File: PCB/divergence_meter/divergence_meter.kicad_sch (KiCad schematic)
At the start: 20 parts, among them U1 74HC595, U2 74HC595, U3 ULN2803A, U4 ULN2803A

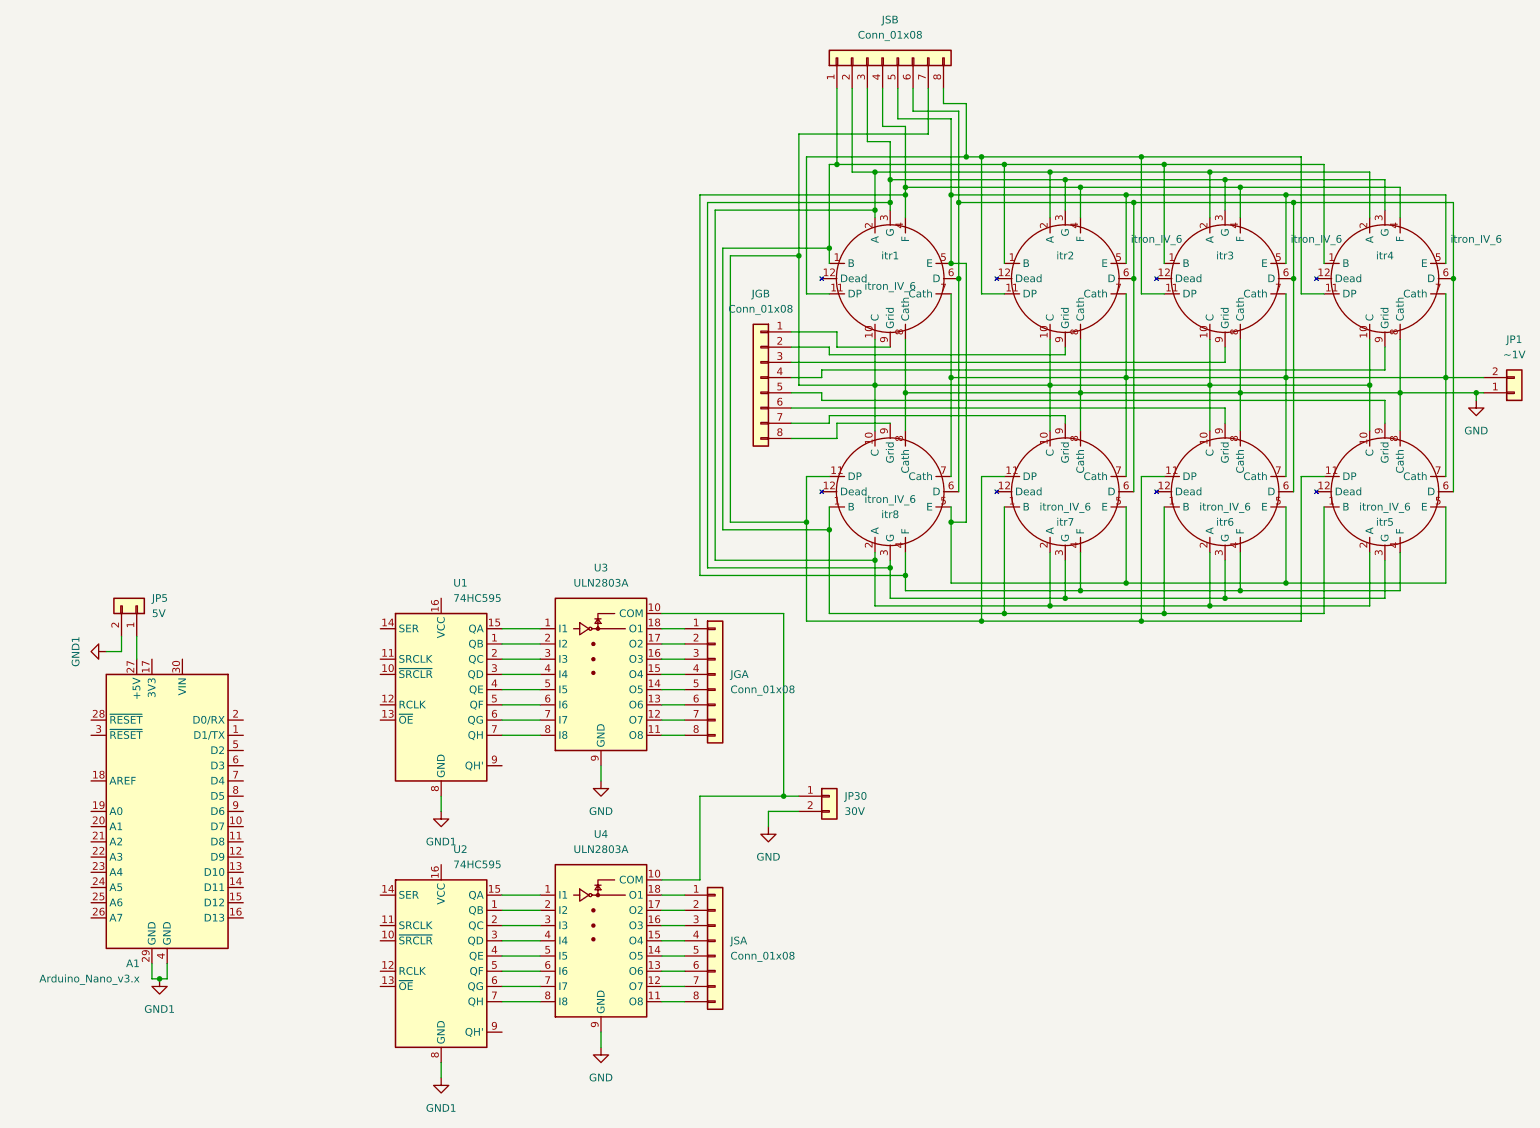
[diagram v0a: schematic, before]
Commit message: Finished schematics, started PCB design
Some schematics changes may be added
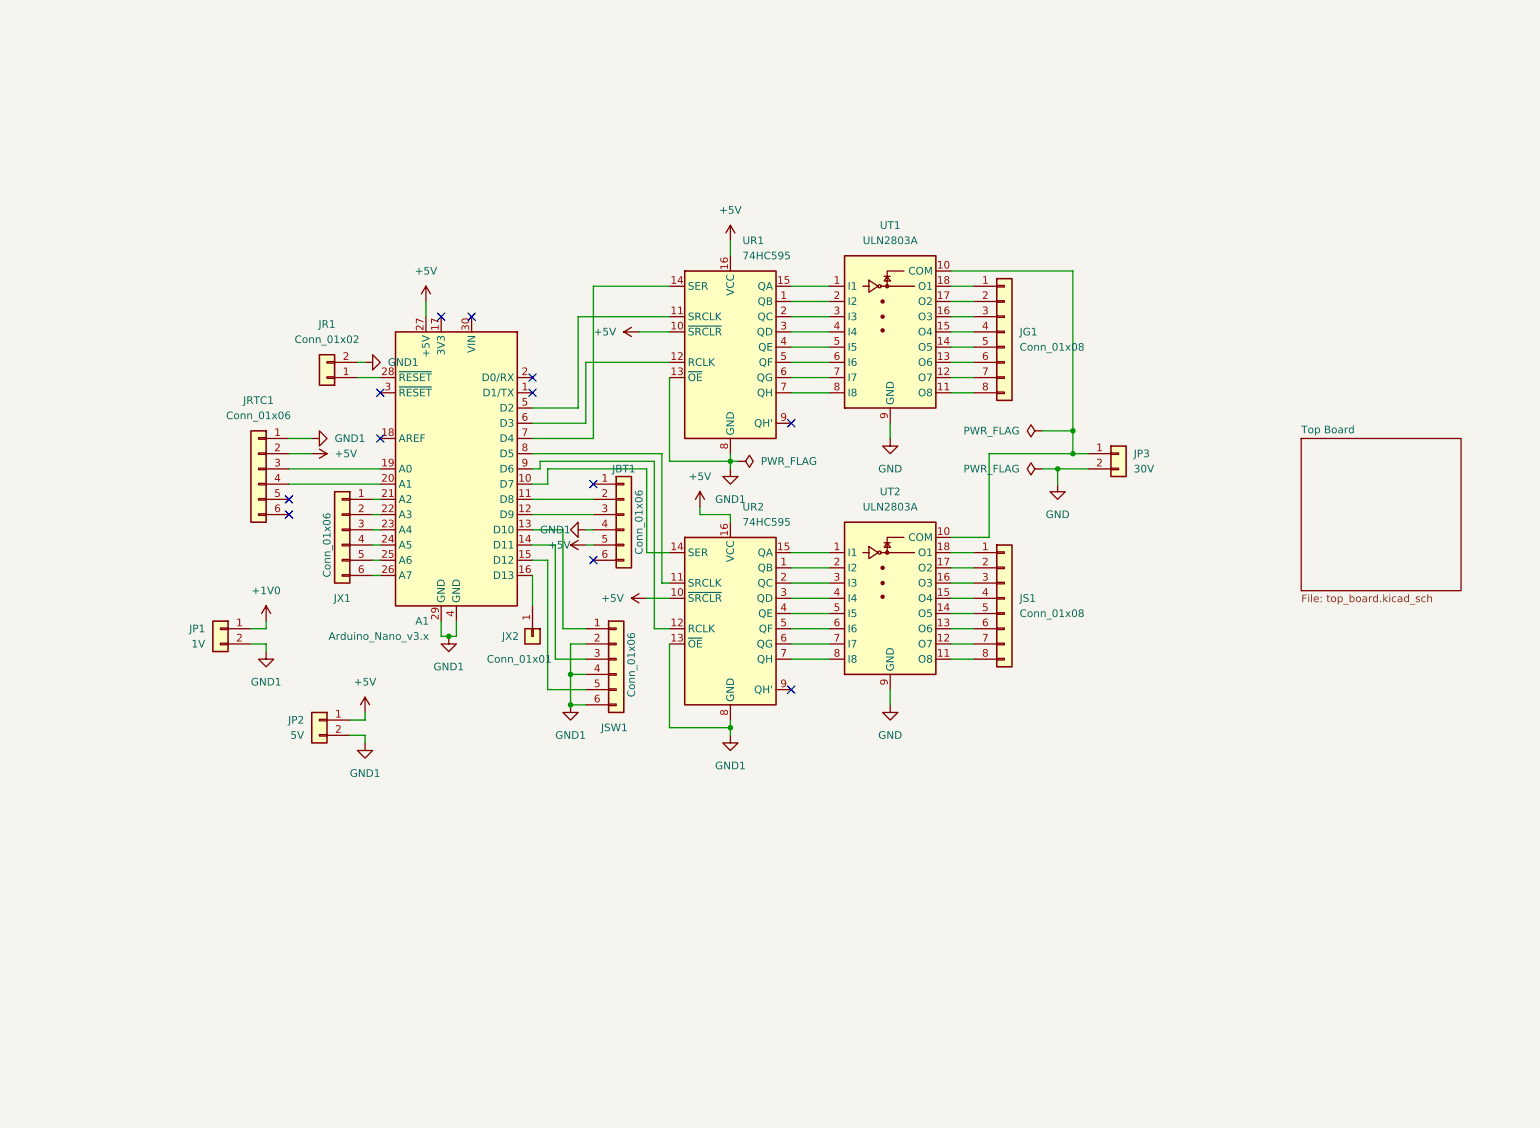
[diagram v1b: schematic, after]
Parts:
- removed JGB, JSB: Conn_01x08, symbol Connector_Generic:Conn_01x08
- removed itr1, itr2, itr3, itr4, itr5, itr6, itr7, itr8: itron_IV_6, symbol divergence:itron_IV_6
- added JBT1, JRTC1: Conn_01x06, Connector_PinSocket_1.27mm:PinSocket_1x06_P1.27mm_Vertical, symbol Connector_Generic:Conn_01x06
- added JR1: Conn_01x02, Connector_PinHeader_1.27mm:PinHeader_1x02_P1.27mm_Vertical, symbol Connector_Generic:Conn_01x02
- added JSW1, JX1: Conn_01x06, Connector_PinHeader_1.27mm:PinHeader_1x06_P1.27mm_Vertical, symbol Connector_Generic:Conn_01x06
- added JX2: Conn_01x01, Connector_PinHeader_1.27mm:PinHeader_1x01_P1.27mm_Vertical, symbol Connector_Generic:Conn_01x01
- JG1: renamed from JGA; footprint (none) -> Connector_PinHeader_1.27mm:PinHeader_1x08_P1.27mm_Vertical
- JP1: value ~1V -> 1V
- JS1: renamed from JSA; footprint (none) -> Connector_PinHeader_1.27mm:PinHeader_1x08_P1.27mm_Vertical
- UR1: renamed from U1; footprint (none) -> SN74HC595N:DIP794W53P254L1930H508Q16N
- UR2: renamed from U2; footprint (none) -> SN74HC595N:DIP794W53P254L1930H508Q16N
- UT1: renamed from U3; footprint (none) -> ULN2803A:DIP850W46P254L2324H393Q18N
- UT2: renamed from U4; footprint (none) -> ULN2803A:DIP850W46P254L2324H393Q18N
- renumbered JP5 to JP2, JP30 to JP3
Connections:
- net GND: no longer JP1.1 (Pin_1)
- net GND1: now also JP1.2 (Pin_2), UR1.13 (~{OE}), UR2.13 (~{OE}), JBT1.4 (Pin_4), JR1.2 (Pin_2), JRTC1.1 (Pin_1), JSW1.2 (Pin_2), JSW1.4 (Pin_4), JSW1.6 (Pin_6)
- net at A1.10 (D7): now also UR2.14 (SER)
- net at A1.11 (D8): now also JBT1.2 (Pin_2)
- net at A1.12 (D9): now also JBT1.3 (Pin_3)
- net at A1.13 (D10): now also JSW1.1 (Pin_1)
- net at A1.14 (D11): now also JSW1.3 (Pin_3)
- net at A1.15 (D12): now also JSW1.5 (Pin_5)
- net at A1.16 (D13): now also JX2.1 (Pin_1)
- net at A1.19 (A0): now also JRTC1.3 (Pin_3)
- net at A1.20 (A1): now also JRTC1.4 (Pin_4)
- net at A1.21 (A2): now also JX1.1 (Pin_1)
- net at A1.22 (A3): now also JX1.2 (Pin_2)
- net at A1.23 (A4): now also JX1.3 (Pin_3)
- net at A1.24 (A5): now also JX1.4 (Pin_4)
- net at A1.25 (A6): now also JX1.5 (Pin_5)
- net at A1.26 (A7): now also JX1.6 (Pin_6)
- net +5V: now reaches A1.27 (+5V), JP2.1 (Pin_1)
- net +5V: now also UR1.10 (~{SRCLR}), UR1.16 (VCC), UR2.10 (~{SRCLR}), UR2.16 (VCC), JBT1.5 (Pin_5), JRTC1.2 (Pin_2)
- net at A1.28 (~{RESET}): now also JR1.1 (Pin_1)
- net at A1.5 (D2): now also UR1.11 (SRCLK)
- net at A1.6 (D3): now also UR1.12 (RCLK)
- net at A1.7 (D4): now also UR1.14 (SER)
- net at A1.8 (D5): now also UR2.11 (SRCLK)
- net at A1.9 (D6): now also UR2.12 (RCLK)
- new net +1V0: JP1.1 (Pin_1)
- no-connect marks 0 -> 12
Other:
- added sheet Top Board (top_board.kicad_sch)
- company: (none) -> Projected by Toohka / Okarisu
- title: (none) -> Divergence Meter - logic board
- moved on the sheet: A1, JG1, JP2, JP3, JS1, UR1, UR2, UT1, UT2

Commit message: working on PCB - itron board almost done
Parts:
- added JPX1: Conn_02x04_Odd_Even, Connector_PinHeader_1.27mm:PinHeader_2x04_P1.27mm_Vertical, symbol Connector_Generic:Conn_02x04_Odd_Even
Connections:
- net +5V: now also JPX1.1 (Pin_1), JPX1.3 (Pin_3), JPX1.5 (Pin_5), JPX1.7 (Pin_7)
- net GND1: now also JPX1.2 (Pin_2), JPX1.4 (Pin_4), JPX1.6 (Pin_6), JPX1.8 (Pin_8)
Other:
- moved on the sheet: JP1, JP2

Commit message: itrons done, started logics
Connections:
- net at A1.10 (D7): now also UR2.11 (SRCLK); no longer UR2.14 (SER)
- net at A1.5 (D2): now also UR1.14 (SER); no longer UR1.11 (SRCLK)
- net at A1.7 (D4): now also UR1.11 (SRCLK); no longer UR1.14 (SER)
- net at A1.8 (D5): now also UR2.14 (SER); no longer UR2.11 (SRCLK)
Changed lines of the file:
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@@
   (no_connect (at 59.69 95.25))
   (no_connect (at 59.69 92.71))
+  (wire (pts (xy 120.65 86.36) (xy 120.65 106.68))
+    (stroke (width 0) (type default) (color 0 0 0 0))
+  )
   (wire (pts (xy 123.19 130.81) (xy 133.35 130.81))
     (stroke (width 0) (type default) (color 0 0 0 0))
   )
-  (wire (pts (xy 123.19 114.3) (xy 120.65 114.3))
-    (stroke (width 0) (type default) (color 0 0 0 0))
-  )
   (wire (pts (xy 170.18 62.23) (xy 173.99 62.23))
     (stroke (width 0) (type default) (color 0 0 0 0))
@@
     (stroke (width 0) (type default) (color 0 0 0 0))
   )
-  (wire (pts (xy 100.33 87.63) (xy 101.6 87.63))
-    (stroke (width 0) (type default) (color 0 0 0 0))
-  )
   (wire (pts (xy 170.18 114.3) (xy 173.99 114.3))
     (stroke (width 0) (type default) (color 0 0 0 0))
@@
     (stroke (width 0) (type default) (color 0 0 0 0))
   )
-  (wire (pts (xy 123.19 69.85) (xy 109.22 69.85))
+  (wire (pts (xy 100.33 90.17) (xy 104.14 90.17))
     (stroke (width 0) (type default) (color 0 0 0 0))
   )
@@
     (stroke (width 0) (type default) (color 0 0 0 0))
   )
+  (wire (pts (xy 109.22 82.55) (xy 100.33 82.55))
+    (stroke (width 0) (type default) (color 0 0 0 0))
+  )
   (wire (pts (xy 102.87 102.87) (xy 100.33 102.87))
     (stroke (width 0) (type default) (color 0 0 0 0))
@@
     (stroke (width 0) (type default) (color 0 0 0 0))
   )
-  (wire (pts (xy 123.19 101.6) (xy 119.38 101.6))
+  (wire (pts (xy 119.38 87.63) (xy 119.38 114.3))
     (stroke (width 0) (type default) (color 0 0 0 0))
   )
@@
     (stroke (width 0) (type default) (color 0 0 0 0))
   )
+  (wire (pts (xy 121.92 85.09) (xy 121.92 101.6))
+    (stroke (width 0) (type default) (color 0 0 0 0))
+  )
   (wire (pts (xy 143.51 64.77) (xy 149.86 64.77))
     (stroke (width 0) (type default) (color 0 0 0 0))
@@
     (stroke (width 0) (type default) (color 0 0 0 0))
   )
-  (wire (pts (xy 119.38 109.22) (xy 123.19 109.22))
+  (wire (pts (xy 116.84 109.22) (xy 123.19 109.22))
     (stroke (width 0) (type default) (color 0 0 0 0))
   )
@@
     (stroke (width 0) (type default) (color 0 0 0 0))
   )
-  (wire (pts (xy 101.6 87.63) (xy 101.6 86.36))
-    (stroke (width 0) (type default) (color 0 0 0 0))
-  )
   (wire (pts (xy 60.96 107.95) (xy 60.96 109.22))
     (stroke (width 0) (type default) (color 0 0 0 0))
@@
     (stroke (width 0) (type default) (color 0 0 0 0))
   )
+  (wire (pts (xy 109.22 62.23) (xy 123.19 62.23))
+    (stroke (width 0) (type default) (color 0 0 0 0))
+  )
   (wire (pts (xy 170.18 74.93) (xy 173.99 74.93))
     (stroke (width 0) (type default) (color 0 0 0 0))
@@
     (stroke (width 0) (type default) (color 0 0 0 0))
   )
-  (wire (pts (xy 123.19 62.23) (xy 107.95 62.23))
-    (stroke (width 0) (type default) (color 0 0 0 0))
-  )
-  (wire (pts (xy 120.65 86.36) (xy 120.65 114.3))
-    (stroke (width 0) (type default) (color 0 0 0 0))
-  )
   (wire (pts (xy 190.5 85.09) (xy 193.04 85.09))
     (stroke (width 0) (type default) (color 0 0 0 0))
@@
     (stroke (width 0) (type default) (color 0 0 0 0))
   )
+  (wire (pts (xy 110.49 69.85) (xy 123.19 69.85))
+    (stroke (width 0) (type default) (color 0 0 0 0))
+  )
   (wire (pts (xy 85.09 113.03) (xy 85.09 115.57))
     (stroke (width 0) (type default) (color 0 0 0 0))
@@
     (stroke (width 0) (type default) (color 0 0 0 0))
   )
-  (wire (pts (xy 121.92 106.68) (xy 121.92 85.09))
-    (stroke (width 0) (type default) (color 0 0 0 0))
-  )
   (wire (pts (xy 143.51 69.85) (xy 149.86 69.85))
     (stroke (width 0) (type default) (color 0 0 0 0))
@@
     (stroke (width 0) (type default) (color 0 0 0 0))
   )
+  (wire (pts (xy 123.19 101.6) (xy 121.92 101.6))
+    (stroke (width 0) (type default) (color 0 0 0 0))
+  )
   (wire (pts (xy 170.18 106.68) (xy 173.99 106.68))
     (stroke (width 0) (type default) (color 0 0 0 0))
@@
     (stroke (width 0) (type default) (color 0 0 0 0))
   )
-  (wire (pts (xy 119.38 87.63) (xy 119.38 101.6))
+  (wire (pts (xy 104.14 90.17) (xy 104.14 86.36))
     (stroke (width 0) (type default) (color 0 0 0 0))
   )
@@
     (stroke (width 0) (type default) (color 0 0 0 0))
   )
-  (wire (pts (xy 107.95 62.23) (xy 107.95 77.47))
+  (wire (pts (xy 107.95 57.15) (xy 107.95 77.47))
     (stroke (width 0) (type default) (color 0 0 0 0))
   )
@@
     (stroke (width 0) (type default) (color 0 0 0 0))
   )
-  (wire (pts (xy 110.49 57.15) (xy 110.49 82.55))
-    (stroke (width 0) (type default) (color 0 0 0 0))
-  )
   (wire (pts (xy 73.66 102.87) (xy 74.93 102.87))
     (stroke (width 0) (type default) (color 0 0 0 0))
@@
     (stroke (width 0) (type default) (color 0 0 0 0))
   )
-  (wire (pts (xy 102.87 87.63) (xy 119.38 87.63))
+  (wire (pts (xy 100.33 87.63) (xy 119.38 87.63))
     (stroke (width 0) (type default) (color 0 0 0 0))
   )
@@
     (stroke (width 0) (type default) (color 0 0 0 0))
   )
+  (wire (pts (xy 110.49 80.01) (xy 110.49 69.85))
+    (stroke (width 0) (type default) (color 0 0 0 0))
+  )
   (wire (pts (xy 160.02 80.01) (xy 160.02 82.55))
     (stroke (width 0) (type default) (color 0 0 0 0))
   )
+  (wire (pts (xy 119.38 114.3) (xy 123.19 114.3))
+    (stroke (width 0) (type default) (color 0 0 0 0))
+  )
   (wire (pts (xy 170.18 109.22) (xy 173.99 109.22))
     (stroke (width 0) (type default) (color 0 0 0 0))
@@
     (stroke (width 0) (type default) (color 0 0 0 0))
   )
+  (wire (pts (xy 107.95 57.15) (xy 123.19 57.15))
+    (stroke (width 0) (type default) (color 0 0 0 0))
+  )
   (wire (pts (xy 133.35 86.36) (xy 134.62 86.36))
     (stroke (width 0) (type default) (color 0 0 0 0))
   )
+  (wire (pts (xy 104.14 86.36) (xy 120.65 86.36))
+    (stroke (width 0) (type default) (color 0 0 0 0))
+  )
   (wire (pts (xy 102.87 124.46) (xy 109.22 124.46))
     (stroke (width 0) (type default) (color 0 0 0 0))
@@
     (stroke (width 0) (type default) (color 0 0 0 0))
   )
-  (wire (pts (xy 102.87 90.17) (xy 102.87 87.63))
-    (stroke (width 0) (type default) (color 0 0 0 0))
-  )
   (wire (pts (xy 118.11 64.77) (xy 123.19 64.77))
     (stroke (width 0) (type default) (color 0 0 0 0))
   )
-  (wire (pts (xy 109.22 69.85) (xy 109.22 80.01))
-    (stroke (width 0) (type default) (color 0 0 0 0))
-  )
-  (wire (pts (xy 123.19 57.15) (xy 110.49 57.15))
-    (stroke (width 0) (type default) (color 0 0 0 0))
-  )
-  (wire (pts (xy 109.22 80.01) (xy 100.33 80.01))
-    (stroke (width 0) (type default) (color 0 0 0 0))
-  )
-  (wire (pts (xy 100.33 90.17) (xy 102.87 90.17))
+  (wire (pts (xy 109.22 62.23) (xy 109.22 82.55))
     (stroke (width 0) (type default) (color 0 0 0 0))
   )
@@
     (stroke (width 0) (type default) (color 0 0 0 0))
   )
+  (wire (pts (xy 100.33 80.01) (xy 110.49 80.01))
+    (stroke (width 0) (type default) (color 0 0 0 0))
+  )
   (wire (pts (xy 133.35 95.25) (xy 133.35 96.52))
     (stroke (width 0) (type default) (color 0 0 0 0))
@@
     (stroke (width 0) (type default) (color 0 0 0 0))
   )
+  (wire (pts (xy 123.19 106.68) (xy 120.65 106.68))
+    (stroke (width 0) (type default) (color 0 0 0 0))
+  )
   (wire (pts (xy 123.19 86.36) (xy 133.35 86.36))
     (stroke (width 0) (type default) (color 0 0 0 0))
@@
     (stroke (width 0) (type default) (color 0 0 0 0))
   )
-  (wire (pts (xy 110.49 82.55) (xy 100.33 82.55))
-    (stroke (width 0) (type default) (color 0 0 0 0))
-  )
-  (wire (pts (xy 101.6 86.36) (xy 120.65 86.36))
-    (stroke (width 0) (type default) (color 0 0 0 0))
-  )
   (wire (pts (xy 170.18 101.6) (xy 173.99 101.6))
     (stroke (width 0) (type default) (color 0 0 0 0))
@@
   )
   (wire (pts (xy 170.18 69.85) (xy 173.99 69.85))
-    (stroke (width 0) (type default) (color 0 0 0 0))
-  )
-  (wire (pts (xy 123.19 106.68) (xy 121.92 106.68))
     (stroke (width 0) (type default) (color 0 0 0 0))
   )
@@
     (pin "1")
   )
-  (symbol (lib_id "power:+5V") (at 119.38 109.22 90) (unit 1)
-    (in_bom yes) (on_board yes) (fields_autoplaced)
-    (property "Reference" "#PWR0110" (id 0) (at 123.19 109.22 0)
-      (effects (font (size 1.27 1.27)) hide)
-    )
-    (property "Value" "+5V" (id 1) (at 115.57 109.2199 90)
-      (effects (font (size 1.27 1.27)) (justify left))
-    )
-    (property "Footprint" "" (id 2) (at 119.38 109.22 0)
-      (effects (font (size 1.27 1.27)) hide)
-    )
-    (property "Datasheet" "" (id 3) (at 119.38 109.22 0)
-      (effects (font (size 1.27 1.27)) hide)
-    )
+  (symbol (lib_id "power:+5V") (at 116.84 109.22 90) (unit 1)
+    (in_bom yes) (on_board yes) (fields_autoplaced)
+    (property "Reference" "#PWR0110" (id 0) (at 120.65 109.22 0)
+      (effects (font (size 1.27 1.27)) hide)
+    )
+    (property "Value" "+5V" (id 1) (at 113.03 109.2199 90)
+      (effects (font (size 1.27 1.27)) (justify left))
+    )
+    (property "Footprint" "" (id 2) (at 116.84 109.22 0)
+      (effects (font (size 1.27 1.27)) hide)
+    )
+    (property "Datasheet" "" (id 3) (at 116.84 109.22 0)
+      (effects (font (size 1.27 1.27)) hide)
+    )
